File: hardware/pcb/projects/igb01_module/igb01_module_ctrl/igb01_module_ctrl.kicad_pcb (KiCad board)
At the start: 2 copper layers, 131 x 111.1 mm, 276 parts, among them J1 ST_JACK_MIDI_OUT, J10 JACK_MAIN_L_OUT, J11 JACK_MAIN_R_OUT, J12 ST_JACK_MIDI_IN, J13 JACK_RST_OUT, J14 JACK_CV_Y_IN, J15 JACK_CV_E_OUT, J16 JACK_CV_F_OUT, J17 JACK_CV_G_OUT, J18 JACK_CV_H_OUT, J19 JACK_RTN_L_IN, J2 JACK_CLK_OUT, J20 JACK_RTN_R_IN, J21 JACK_SND_L_OUT, J22 JACK_SND_R_OUT, J23 JTAG, J24 LEFT_CON, J25 RIGHT_CON, J27 SWD_CON, J28 DISP_CON1, J29 Micro_SD_Card, J3 JACK_CV_X_IN, J30 Conn_01x03, J31 Conn_01x03, J32 Conn_01x03, J33 POWER_CON, J4 JACK_CV_A_OUT, J5 JACK_CV_B_OUT, J6 JACK_CV_C_OUT, J7 JACK_CV_D_OUT, J8 JACK_EXT_L_IN, J9 JACK_EXT_R_IN, SW1 SW_Push_45deg, SW10 SW_Push_45deg, SW11 SW_Push_45deg, SW12 SW_Push_45deg, SW13 SW_Push_45deg, SW14 SW_Push_45deg, SW15 SW_Push_45deg, SW16 SW_Push_45deg, SW17 SW_Push_45deg, SW18 SW_Push_45deg, SW19 SW_Push_45deg, SW2 SW_Push_45deg, SW20 SW_Push_45deg, SW21 SW_Push_45deg, SW22 SW_Push_45deg, SW23 SW_Push_45deg, SW24 SW_Push_45deg, SW25 SW_Push_45deg, SW26 SW_Push_45deg, SW27 SW_Push_45deg, SW28 SW_Push_45deg, SW29 SW_Push_45deg, SW3 SW_Push_45deg, SW30 SW_Push_45deg, SW31 SW_Push_45deg, SW32 SW_Push_45deg, SW33 SW_Push_45deg, SW34 SW_Push_45deg, SW35 SW_Push_45deg, SW36 SW_Push_45deg, SW4 SW_Push_45deg, SW5 SW_Push_45deg, SW6 SW_Push_45deg, SW7 SW_Push_45deg, SW8 SW_Push_45deg, SW9 SW_Push_45deg, U1 TL074, U10 STM32G431RBTx, U11 TL074, U12 R-78B5.0-2.0, U13 LDK320-3.3V, U14 LDK320-3.3V, U15 LM4040DBZ-10, U2 TL074, U3 74AHCT1G125, U4 TLP2361, U5 74AHCT1G125, U6 74AHCT1G125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

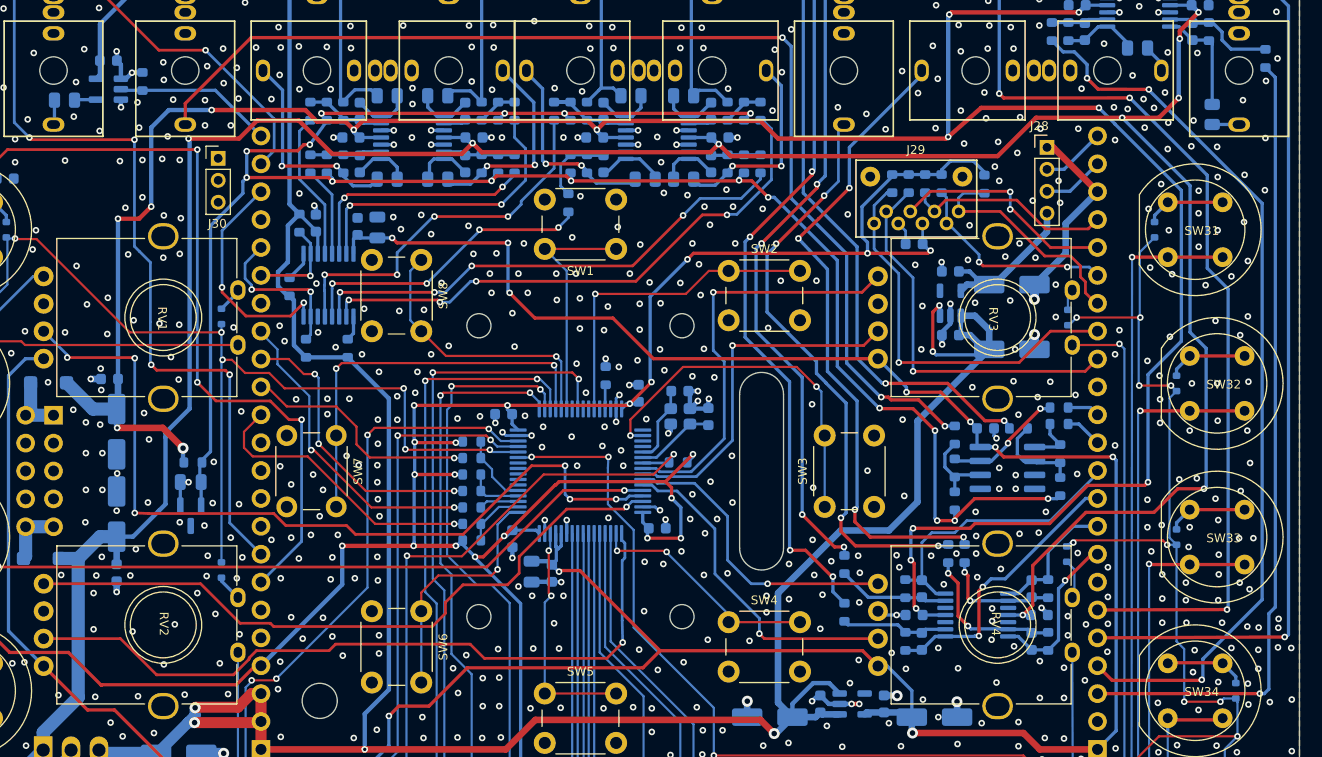
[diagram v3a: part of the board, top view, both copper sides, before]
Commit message: add igb01 module led board
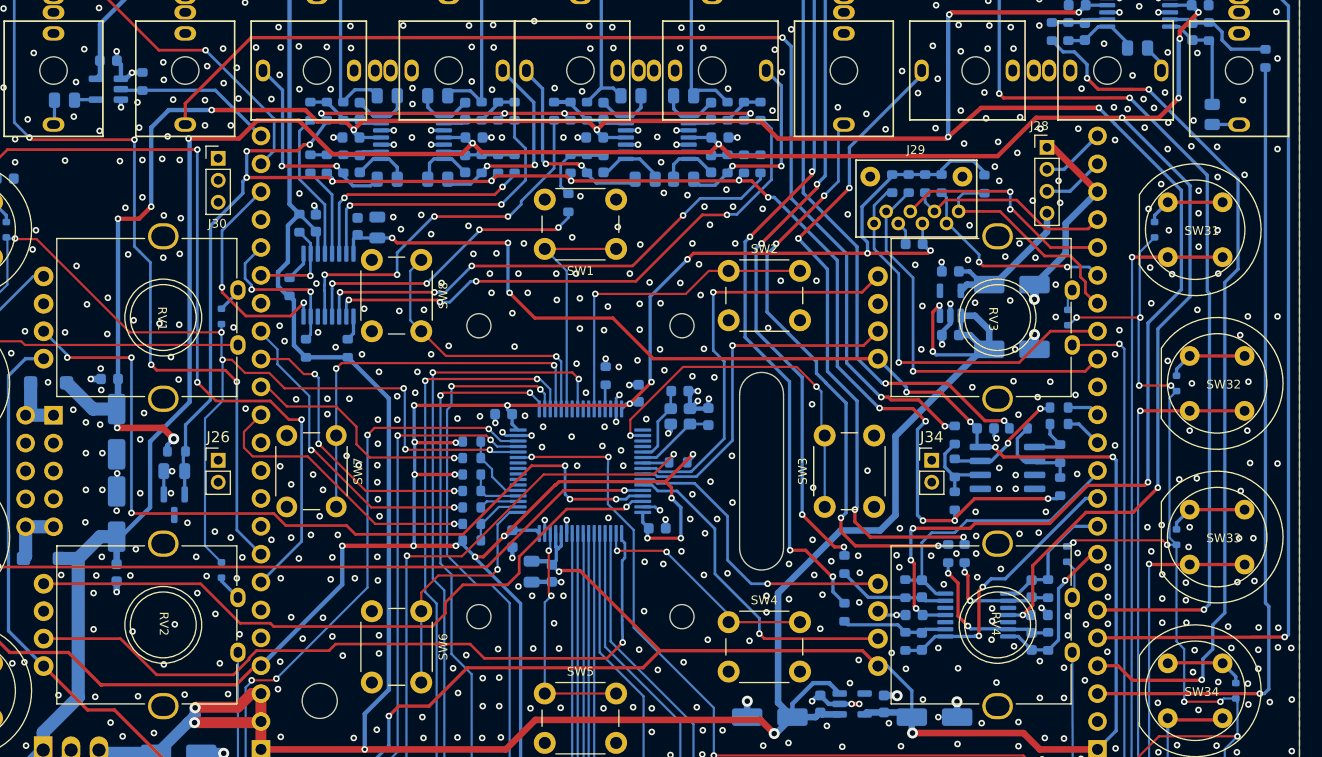
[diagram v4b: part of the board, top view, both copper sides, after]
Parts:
- added J26: Conn_01x02, Connector_PinHeader_2.00mm:PinHeader_1x02_P2.00mm_Vertical, F.Cu at (82.5, 103.0)
- added J34: Conn_01x02, Connector_PinHeader_2.00mm:PinHeader_1x02_P2.00mm_Vertical, F.Cu at (147.5, 103.0)
- moved C56 1.80 mm to (78.5, 104.0)
- moved R88 1.80 mm to (78.7, 102.2)
- moved U15 1.80 mm to (78.5, 107.0)
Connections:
- J31 pad 1: unconnected-(J31-Pin_1-Pad1) -> GND
- J31 pad 2: unconnected-(J31-Pin_2-Pad2) -> GND
- J31 pad 3: unconnected-(J31-Pin_3-Pad3) -> GND
- J32 pad 1: unconnected-(J32-Pin_1-Pad1) -> GND
- J32 pad 2: unconnected-(J32-Pin_2-Pad2) -> GND
- J32 pad 3: unconnected-(J32-Pin_3-Pad3) -> GND
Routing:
- net +12V: track 251.9 -> 247.5 mm
- net /OUT1L: track 89.7 -> 87.1 mm
- net /OUT2L: track 81.8 -> 80.0 mm
- net /BTN_MUX_C: track 149.5 -> 150.7 mm
- net -12V: track 237.5 -> 236.4 mm
- net /VREF_-10V: track 188.5 -> 189.4 mm
- net GND: vias 1024 -> 1005
